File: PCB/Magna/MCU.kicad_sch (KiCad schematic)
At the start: 35 parts, among them J701 Conn_02x06_Odd_Even, J702 Conn_02x06_Odd_Even, J703 Conn_ARM_JTAG_SWD_20, J704 Boot Jumper, U701 STM32F730V8T6, Y701 24MHz

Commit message: Update Audio connector pinning (#14)
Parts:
- removed J702: Conn_02x06_Odd_Even, Connector_PinSocket_2.54mm:PinSocket_2x06_P2.54mm_Vertical_SMD, symbol Connector_Generic:Conn_02x06_Odd_Even
- removed R703, R704: 22R, Resistor_SMD:R_0805_2012Metric_Pad1.20x1.40mm_HandSolder, symbol Device:R_Small
- added C201: F/NM, Capacitor_SMD:C_0603_1608Metric_Pad1.08x0.95mm_HandSolder, symbol Device:C
- added R201: R/NM, Resistor_SMD:R_0805_2012Metric_Pad1.20x1.40mm_HandSolder, symbol Device:R_Small
- added R202: R/NM, Resistor_SMD:R_0805_2012Metric_Pad1.20x1.40mm_HandSolder, symbol Device:R
- added R203, R204, R205, R206, R207, R212: 22R, Resistor_SMD:R_0805_2012Metric_Pad1.20x1.40mm_HandSolder, symbol Device:R_Small
- added R208, R209, R210, R211, R213, R214, R215, R216: 0R, Resistor_SMD:R_0805_2012Metric_Pad1.20x1.40mm_HandSolder, symbol Device:R_Small
- added TP201: TestPoint, TestPoint:TestPoint_Keystone_5005-5009_Compact, symbol Connector:TestPoint
- added U201: 24.576 MHz, Oscillator:Oscillator_SMD_Abracon_ASE-4Pin_3.2x2.5mm_HandSoldering, symbol Oscillator:ECS-2520MV-xxx-xx
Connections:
- net BCLK: now also R204.1, R215.2, R216.2
- net BCLK_MCU: now also R204.2
- net GND: now also C201.2, R202.2, U201.2 (GND)
- net I2S2_BCLK: now also R215.1
- net I2S2_LRCLK: now also R214.1
- net I2S3_BCLK: now also R216.1
- net I2S3_LRCLK: now also R213.1
- net LRCLK: now also R205.1, R213.2, R214.2
- net LRCLK_MCU: now also R205.2
- net MCLK: now also R203.1, R212.1; no longer U701.66 (PC9)
- net USB_PHY_RESET: now also U701.8 (PC14-OSC32_IN); no longer U701.7 (PC13)
- net VDD: now also R201.1, U201.4 (VDD)
- net serial_data: now also R706.2; no longer R706.1
- net ~{HSW_EN}: now also U701.7 (PC13); no longer U701.1 (PE2)
- net at U701.44 (PE14): now also R706.1; no longer R706.2
- net AudioAdc0 renamed ADC_DATA_0_MCU
- net ADC_DATA_0_MCU: now also R208.1
- net AudioAdc1 renamed ADC_DATA_1_MCU
- net ADC_DATA_1_MCU: now also R209.1
- net AudioDac0 renamed ADC_DATA_2_MCU
- net ADC_DATA_2_MCU: now also R210.1
- net AudioDac1 renamed ADC_DATA_3_MCU
- net ADC_DATA_3_MCU: now also R211.1
- net I2S2_SD renamed DAC_DATA_0_MCU
- net DAC_DATA_0_MCU: now also R206.2
- net I2S3_SD renamed DAC_DATA_1_MCU
- net DAC_DATA_1_MCU: now also R207.2
- new net: R201.2, U201.1 (Tri-State)
- new net ADC_DATA_0: R208.2
- new net ADC_DATA_1: R209.2
- new net ADC_DATA_2: R210.2
- new net ADC_DATA_3: R211.2
- new net DAC_DATA_0: R206.1
- new net DAC_DATA_1: R207.1
- new net MCLK_24.576MHz: C201.1, R202.1, R212.2, TP201.1, U201.3 (OUT), U701.66 (PC9)
- new net MCU_MCLK_OUT: R203.2, U701.1 (PE2)
- no-connect marks 13 -> 12
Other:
- note added: "MCLK Generation and distribution"
- note removed: "IS2 expansion header"
- moved on the sheet: R701, R702, R706

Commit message: Update connector on ADC board and clean up MCU sheet
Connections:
- net VA_en renamed VAA_EN
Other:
- note added: "I2S Bus and Pins"
- moved on the sheet: C201, J703, R201, R202, R203, R204, R205, R206, R207, R208, R209, R210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

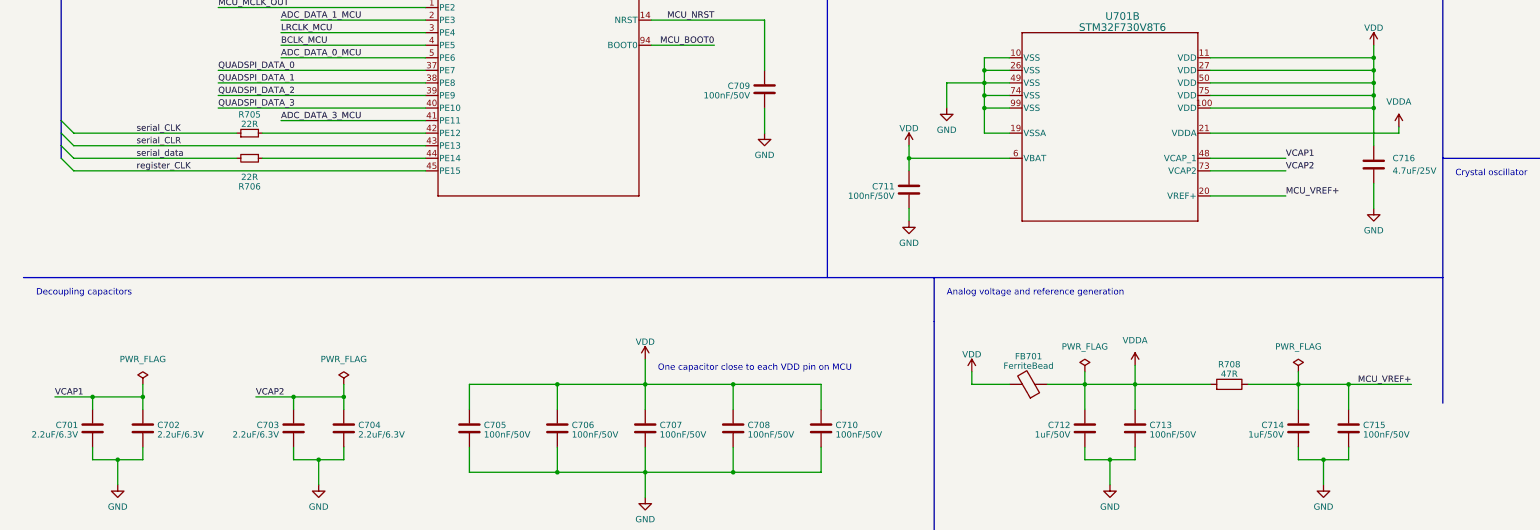
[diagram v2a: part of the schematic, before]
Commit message: Change components on Main Board to use more of the same part#
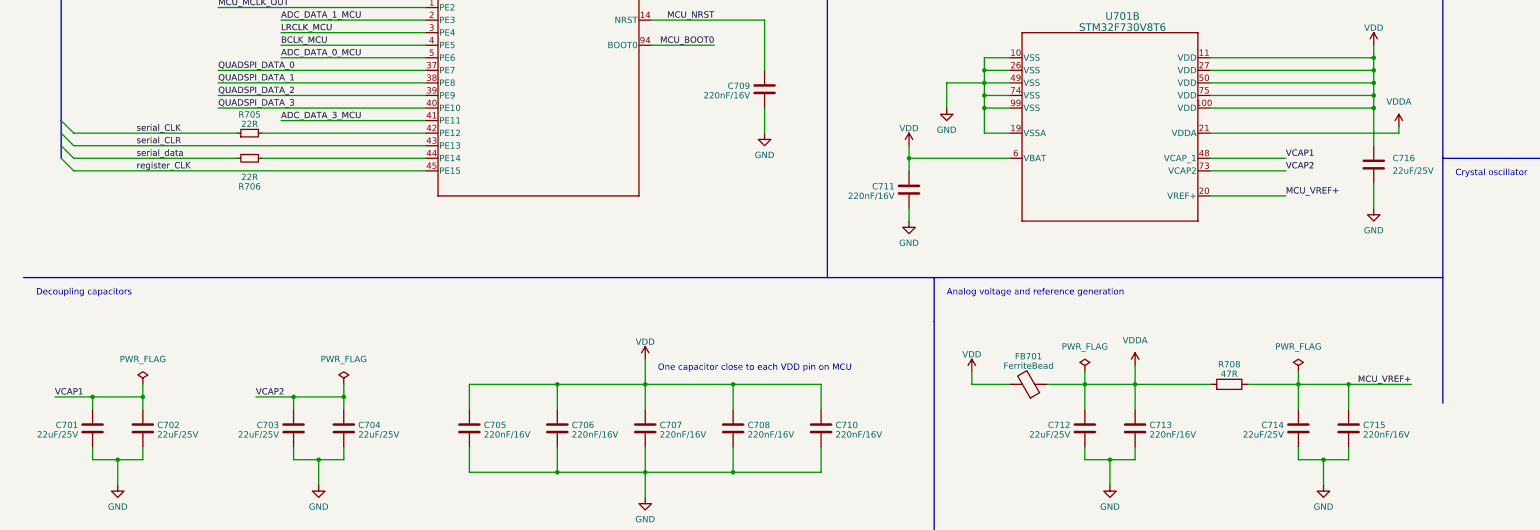
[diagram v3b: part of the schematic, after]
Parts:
- C201: footprint Capacitor_SMD:C_0603_1608Metric_Pad1.08x0.95mm_HandSolder -> Capacitor_SMD:C_0805_2012Metric_Pad1.18x1.45mm_HandSolder
- C701, C702, C703, C704: value 2.2uF/6.3V -> 22uF/25V; LCSC C377773 -> C45783
- C705, C706, C707, C708, C709, C710, C711, C713, C715: value 100nF/50V -> 220nF/16V; footprint Capacitor_SMD:C_0805_2012Metric_Pad1.18x1.45mm_HandSolder -> Capacitor_SMD:C_0402_1005Metric_Pad0.74x0.62mm_HandSolder; LCSC C49678 -> C16772
- C712, C714: value 1uF/50V -> 22uF/25V; LCSC C28323 -> C45783
- C716: value 4.7uF/25V -> 22uF/25V; LCSC C1779 -> C45783
- TP201: footprint TestPoint:TestPoint_Keystone_5005-5009_Compact -> TestPoint:TestPoint_Keystone_5000-5004_Miniature

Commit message: Add more traces to the PCB
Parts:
- added C212: 22uF/25V, Capacitor_SMD:C_0805_2012Metric_Pad1.18x1.45mm_HandSolder, symbol Device:C
- added R225, R226: 0R, Resistor_SMD:R_0805_2012Metric_Pad1.20x1.40mm_HandSolder, symbol Device:R_Small
- renumbered C701 to C201, C702 to C202, C703 to C203, C704 to C204, C705 to C205, C706 to C206, C707 to C207, C708 to C208, C709 to C209, C710 to C210, C711 to C211, C712 to C213, C713 to C214, C714 to C215, C715 to C216, C716 to C217, C717 to C218, C718 to C219, C201 to C220, FB701 to FB201, J701 to J201, J703 to J202, J704 to J203, R701 to R201, R702 to R202, R705 to R203, R706 to R204, R707 to R205, R708 to R206, R201 to R207, R709 to R208, R215 to R209, R216 to R210, R214 to R211, R213 to R212, R212 to R213, R203 to R214, R204 to R215, R205 to R216, R208 to R217, R209 to R218, R210 to R219, R211 to R220, R206 to R221, R207 to R222, R202 to R223, R710 to R224, U701 to U201, U201 to U202, Y701 to Y201
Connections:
- net ADC_DATA_0: now also R217.1; no longer R217.2
- net ADC_DATA_0_MCU: now also R217.2; no longer R217.1
- net ADC_DATA_1: now also R218.1; no longer R218.2
- net ADC_DATA_1_MCU: now also R218.2; no longer R218.1
- net ADC_DATA_2: now also R219.1; no longer R219.2
- net ADC_DATA_2_MCU: now also R219.2; no longer R219.1
- net ADC_DATA_3: now also R220.1; no longer R220.2
- net ADC_DATA_3_MCU: now also R220.2; no longer R220.1
- net GND: now also C212.2
- net VDD: now also C212.1
- net lsb: now also R225.2; no longer U201.59 (PD12)
- net msb: now also R226.1; no longer U201.60 (PD13)
- new net: R225.1, U201.59 (PD12)
- new net: R226.2, U201.60 (PD13)
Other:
- moved on the sheet: FB201, R217, R218, R219, R220

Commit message: More routing
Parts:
- added C221: 220nF/16V, Capacitor_SMD:C_0402_1005Metric_Pad0.74x0.62mm_HandSolder, symbol Device:C
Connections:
- net ADC_FORMAT: now also U201.61 (PD14); no longer U201.55 (PD8)
- net ADC_M/S: now also U201.62 (PD15); no longer U201.56 (PD9)
- net BCLK: now also R209.1, R210.1; no longer R209.2, R210.2
- net GND: now also C221.2
- net I2S2_BCLK: now also R209.2; no longer R209.1
- net I2S2_LRCLK: now also R211.2; no longer R211.1
- net I2S3_BCLK: now also R210.2; no longer R210.1
- net I2S3_LRCLK: now also R212.2; no longer R212.1
- net LRCLK: now also R211.1, R212.1; no longer R211.2, R212.2
- net MIDI_RX: now also U201.56 (PD9); no longer U201.83 (PD2)
- net MIDI_TX: now also U201.55 (PD8); no longer U201.80 (PC12)
- net VDD: now also C221.1
- net USB_HOST_MCU_N: now reaches R201.2, U201.70 (PA11)
- net USB_HOST_MCU_P: now reaches R202.2, U201.71 (PA12)
- net serial_CLK_MCU: now reaches R203.2, U201.42 (PE12)
- net serial_data_MCU: now reaches R204.1, U201.44 (PE14)
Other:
- moved on the sheet: C220, R207, R209, R210, R211, R212, R223, R225, R226, TP201, U202

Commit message: Add last routing
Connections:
- net GND: now also J201.2 (Pin_2), J201.6 (Pin_6); no longer J201.12 (Pin_12), J201.8 (Pin_8)
- net QUADSPI_CLK: now also J201.1 (Pin_1); no longer J201.6 (Pin_6)
- net QUADSPI_DATA_2: now also J201.7 (Pin_7); no longer J201.2 (Pin_2)
- net QUADSPI_DATA_3: now also J201.9 (Pin_9); no longer J201.4 (Pin_4)
- net QUADSPI_NCS: now also J201.11 (Pin_11); no longer J201.7 (Pin_7)
- net VDD: now also J201.12 (Pin_12), J201.4 (Pin_4), J201.8 (Pin_8); no longer J201.1 (Pin_1), J201.11 (Pin_11), J201.9 (Pin_9)
- net ~{HSW_EN}: now also U201.69 (PA10); no longer U201.7 (PC13)
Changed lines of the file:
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@@
   (bus_alias "USB_HS_ULPI" (members "STP" "DIR" "NXT" "DATA0" "DATA1" "DATA2" "DATA3" "DATA4" "DATA5" "DATA6" "DATA7" "CLK"))
   (bus_alias "pot_select" (members "lsb" "msb"))
-  (junction (at 280.67 58.42) (diameter 0) (color 0 0 0 0)
-  )
   (junction (at 227.33 248.92) (diameter 0) (color 0 0 0 0)
   )
@@
   (junction (at 351.79 229.87) (diameter 0) (color 0 0 0 0)
   )
+  (junction (at 276.86 53.34) (diameter 0) (color 0 0 0 0)
+  )
   (junction (at 361.95 151.13) (diameter 0) (color 0 0 0 0)
   )
@@
   (junction (at 232.41 264.16) (diameter 0) (color 0 0 0 0)
   )
+  (junction (at 276.86 48.26) (diameter 0) (color 0 0 0 0)
+  )
   (junction (at 285.75 185.42) (diameter 0) (color 0 0 0 0)
   )
@@
   (junction (at 285.75 187.96) (diameter 0) (color 0 0 0 0)
   )
-  (junction (at 234.95 55.88) (diameter 0) (color 0 0 0 0)
-  )
   (junction (at 275.59 264.16) (diameter 0) (color 0 0 0 0)
   )
@@
   (junction (at 120.65 266.7) (diameter 0) (color 0 0 0 0)
   )
-  (junction (at 234.95 45.72) (diameter 0) (color 0 0 0 0)
-  )
   (junction (at 237.49 248.92) (diameter 0) (color 0 0 0 0)
   )
@@
   (junction (at 264.16 144.78) (diameter 0) (color 0 0 0 0)
   )
+  (junction (at 280.67 50.8) (diameter 0) (color 0 0 0 0)
+  )
   (junction (at 359.41 156.21) (diameter 0) (color 0 0 0 0)
   )
@@
   (no_connect (at 132.08 114.3))
   (no_connect (at 132.08 119.38))
+  (no_connect (at 132.08 99.06))
   (no_connect (at 81.28 83.82))
   (no_connect (at 132.08 134.62))
-  (no_connect (at 81.28 91.44))
   (no_connect (at 132.08 109.22))
   (no_connect (at 132.08 86.36))
@@
     (stroke (width 0) (type default))
   )
-  (wire (pts (xy 280.67 53.34) (xy 280.67 55.88))
+  (wire (pts (xy 280.67 45.72) (xy 280.67 50.8))
     (stroke (width 0) (type default))
   )
@@
     (stroke (width 0) (type default))
   )
-  (wire (pts (xy 252.73 58.42) (xy 234.95 58.42))
-    (stroke (width 0) (type default))
-  )
   (wire (pts (xy 71.12 86.36) (xy 81.28 86.36))
     (stroke (width 0) (type default))
@@
     (stroke (width 0) (type default))
   )
+  (wire (pts (xy 276.86 53.34) (xy 276.86 58.42))
+    (stroke (width 0) (type default))
+  )
   (wire (pts (xy 132.08 142.24) (xy 170.18 142.24))
     (stroke (width 0) (type default))
@@
     (stroke (width 0) (type default))
   )
-  (wire (pts (xy 265.43 58.42) (xy 280.67 58.42))
-    (stroke (width 0) (type default))
-  )
   (wire (pts (xy 270.51 246.38) (xy 270.51 248.92))
     (stroke (width 0) (type default))
@@
     (stroke (width 0) (type default))
   )
-  (wire (pts (xy 252.73 55.88) (xy 234.95 55.88))
-    (stroke (width 0) (type default))
-  )
   (bus (pts (xy 48.26 71.12) (xy 48.26 48.26))
     (stroke (width 0) (type default))
@@
     (stroke (width 0) (type default))
   )
+  (wire (pts (xy 265.43 58.42) (xy 276.86 58.42))
+    (stroke (width 0) (type default))
+  )
   (wire (pts (xy 356.87 158.75) (xy 356.87 161.29))
     (stroke (width 0) (type default))
@@
     (stroke (width 0) (type default))
   )
-  (wire (pts (xy 265.43 45.72) (xy 280.67 45.72))
+  (wire (pts (xy 252.73 53.34) (xy 237.49 53.34))
     (stroke (width 0) (type default))
   )
@@
     (stroke (width 0) (type default))
   )
-  (wire (pts (xy 265.43 50.8) (xy 280.67 50.8))
-    (stroke (width 0) (type default))
-  )
   (wire (pts (xy 156.21 266.7) (xy 138.43 266.7))
     (stroke (width 0) (type default))
@@
     (stroke (width 0) (type default))
   )
+  (wire (pts (xy 276.86 48.26) (xy 276.86 53.34))
+    (stroke (width 0) (type default))
+  )
   (wire (pts (xy 191.77 200.66) (xy 191.77 203.2))
     (stroke (width 0) (type default))
@@
     (stroke (width 0) (type default))
   )
-  (wire (pts (xy 280.67 58.42) (xy 280.67 64.77))
+  (wire (pts (xy 237.49 45.72) (xy 252.73 45.72))
+    (stroke (width 0) (type default))
+  )
+  (wire (pts (xy 280.67 55.88) (xy 280.67 64.77))
     (stroke (width 0) (type default))
   )
@@
     (stroke (width 0) (type default))
   )
+  (wire (pts (xy 265.43 45.72) (xy 280.67 45.72))
+    (stroke (width 0) (type default))
+  )
   (wire (pts (xy 339.09 237.49) (xy 351.79 237.49))
     (stroke (width 0) (type default))
@@
     (stroke (width 0) (type default))
   )
-  (wire (pts (xy 147.32 99.06) (xy 132.08 99.06))
+  (wire (pts (xy 66.04 91.44) (xy 81.28 91.44))
     (stroke (width 0) (type default))
   )
@@
     (stroke (width 0) (type default))
   )
-  (wire (pts (xy 280.67 55.88) (xy 280.67 58.42))
-    (stroke (width 0) (type default))
-  )
   (wire (pts (xy 26.67 251.46) (xy 36.83 251.46))
     (stroke (width 0) (type default))
@@
     (stroke (width 0) (type default))
   )
-  (wire (pts (xy 234.95 38.1) (xy 234.95 45.72))
+  (wire (pts (xy 290.83 198.12) (xy 290.83 196.85))
     (stroke (width 0) (type default))
   )
-  (wire (pts (xy 290.83 198.12) (xy 290.83 196.85))
+  (wire (pts (xy 265.43 48.26) (xy 276.86 48.26))
     (stroke (width 0) (type default))
   )
@@
     (stroke (width 0) (type default))
   )
+  (wire (pts (xy 280.67 50.8) (xy 280.67 55.88))
+    (stroke (width 0) (type default))
+  )
   (polyline (pts (xy 299.72 227.33) (xy 299.72 252.73))
     (stroke (width 0) (type default))
@@
     (stroke (width 0) (type default))
   )
-  (wire (pts (xy 234.95 45.72) (xy 252.73 45.72))
-    (stroke (width 0) (type default))
-  )
   (bus (pts (xy 171.45 68.58) (xy 171.45 71.12))
     (stroke (width 0) (type default))
@@
     (stroke (width 0) (type default))
   )
-  (wire (pts (xy 234.95 58.42) (xy 234.95 55.88))
+  (wire (pts (xy 276.86 38.1) (xy 276.86 48.26))
     (stroke (width 0) (type default))
   )
@@
     (stroke (width 0) (type default))
   )
-  (wire (pts (xy 237.49 53.34) (xy 252.73 53.34))
+  (wire (pts (xy 237.49 58.42) (xy 252.73 58.42))
     (stroke (width 0) (type default))
   )
@@
     (stroke (width 0) (type default))
   )
+  (wire (pts (xy 265.43 53.34) (xy 276.86 53.34))
+    (stroke (width 0) (type default))
+  )
   (wire (pts (xy 204.47 246.38) (xy 204.47 248.92))
     (stroke (width 0) (type default))
@@
     (stroke (width 0) (type default))
   )
-  (wire (pts (xy 265.43 53.34) (xy 280.67 53.34))
-    (stroke (width 0) (type default))
-  )
   (wire (pts (xy 351.79 214.63) (xy 346.71 214.63))
     (stroke (width 0) (type default))
@@
     (stroke (width 0) (type default))
   )
-  (wire (pts (xy 234.95 55.88) (xy 234.95 45.72))
-    (stroke (width 0) (type default))
-  )
   (bus (pts (xy 48.26 139.7) (xy 48.26 137.16))
     (stroke (width 0) (type default))
@@
     (stroke (width 0) (type default))
   )
-  (wire (pts (xy 265.43 48.26) (xy 280.67 48.26))
+  (wire (pts (xy 252.73 55.88) (xy 237.49 55.88))
     (stroke (width 0) (type default))
   )
@@
     (stroke (width 0) (type default))
   )
+  (wire (pts (xy 265.43 50.8) (xy 280.67 50.8))
+    (stroke (width 0) (type default))
+  )
   (polyline (pts (xy 196.85 236.22) (xy 196.85 284.48))
     (stroke (width 0) (type default))
@@
     (effects (font (size 1.27 1.27)) (justify left bottom))
   )
-  (label "QUADSPI_DATA_3" (at 280.67 48.26 180) (fields_autoplaced)
-    (effects (font (size 1.27 1.27)) (justify right bottom))
+  (label "QUADSPI_DATA_3" (at 237.49 55.88 0) (fields_autoplaced)
+    (effects (font (size 1.27 1.27)) (justify left bottom))
   )
   (label "ADC_4" (at 153.67 68.58 180) (fields_autoplaced)
@@
     (effects (font (size 1.27 1.27)) (justify right bottom))
   )
-  (label "QUADSPI_NCS" (at 237.49 53.34 0) (fields_autoplaced)
+  (label "QUADSPI_NCS" (at 237.49 58.42 0) (fields_autoplaced)
     (effects (font (size 1.27 1.27)) (justify left bottom))
   )
@@
     (effects (font (size 1.27 1.27)) (justify left bottom))
   )
-  (label "QUADSPI_CLK" (at 280.67 50.8 180) (fields_autoplaced)
-    (effects (font (size 1.27 1.27)) (justify right bottom))
+  (label "QUADSPI_CLK" (at 237.49 45.72 0) (fields_autoplaced)
+    (effects (font (size 1.27 1.27)) (justify left bottom))
   )
   (label "ADC_DATA_2" (at 349.25 173.99 0) (fields_autoplaced)
@@
     (effects (font (size 1.27 1.27)) (justify left bottom))
   )
-  (label "QUADSPI_DATA_2" (at 280.67 45.72 180) (fields_autoplaced)
-    (effects (font (size 1.27 1.27)) (justify right bottom))
+  (label "QUADSPI_DATA_2" (at 237.49 53.34 0) (fields_autoplaced)
+    (effects (font (size 1.27 1.27)) (justify left bottom))
   )
   (label "ADC_2" (at 57.15 71.12 0) (fields_autoplaced)
@@
     (effects (font (size 1.27 1.27)) (justify right))
   )
-  (hierarchical_label "~{HSW_EN}" (shape output) (at 147.32 99.06 0) (fields_autoplaced)
-    (effects (font (size 1.27 1.27)) (justify left))
+  (hierarchical_label "~{HSW_EN}" (shape output) (at 66.04 91.44 180) (fields_autoplaced)
+    (effects (font (size 1.27 1.27)) (justify right))
   )
   (hierarchical_label "I2C_SCA" (shape bidirectional) (at 30.48 127 180) (fields_autoplaced)
@@
     )
   )
-  (symbol (lib_id "power:VDD") (at 234.95 38.1 0) (unit 1)
+  (symbol (lib_id "power:VDD") (at 276.86 38.1 0) (unit 1)
     (in_bom yes) (on_board yes) (dnp no)
-    (property "Reference" "#PWR0212" (at 234.95 41.91 0)
+    (property "Reference" "#PWR0212" (at 276.86 41.91 0)
       (effects (font (size 1.27 1.27)) hide)
     )
-    (property "Value" "VDD" (at 234.95 34.5981 0)
+    (property "Value" "VDD" (at 276.86 34.5981 0)
       (effects (font (size 1.27 1.27)))
     )
-    (property "Footprint" "" (at 234.95 38.1 0)
+    (property "Footprint" "" (at 276.86 38.1 0)
       (effects (font (size 1.27 1.27)) hide)
     )
-    (property "Datasheet" "" (at 234.95 38.1 0)
+    (property "Datasheet" "" (at 276.86 38.1 0)
       (effects (font (size 1.27 1.27)) hide)
     )
